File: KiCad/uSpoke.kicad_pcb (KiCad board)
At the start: 2 copper layers, 50 x 100 mm, 143 parts, among them J1 B2B-PH-K-S, J10 BL-A, J11 BL-C, J12 Amphenol 132289, J2 BAT+, J3 BAT-, J4 GCT USB4105/USB4110, J5 USB+, J6 USB-, J7 PLS-1x3, J8 PLS-1x6, J9 PLS-1x3, Q1 AO3407A, Q2 AO3407A, Q3 AO3400, Q4 AO3400, Q5 AO3400, Q6 AO3400, U1 SP0503BAHTG, U2 TP4056, U3 CP2102N-A02-GQFN28, U4 LM3671MF-3.3, U5 74HC4052PW, U6 STM32F103C8T6, U7 LSM303DLHC, X1 8MHz

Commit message: Draft PCB
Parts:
- removed A3: GM12864-01A, Spoke:GM12864-01A
- removed A4: G10A-F30, Spoke:G10A-F30
- removed A5: TU10-F, Spoke:TU10-F
- removed C10, C21, C3, C31, C33, C35, C4, C6: 100nF, Spoke:C0603
- removed C12, C9: ~, Spoke:C0603
- removed C2, C32, C7: 4.7uF, Spoke:C0805
- removed C24: 80 mF Supercap, Spoke:XH414HG-IV01E
- removed C29: 47uF, Spoke:C_tantA
- removed C34: 10uF, Spoke:C1206
- removed C36: 220nF, Spoke:C0603
- removed D6: BAT54C, Spoke:SOT-23
- removed H1: MountingHole, MountingHole:MountingHole_3.2mm_M3
- removed Q1: AO3407A, Spoke:SOT-23
- removed Q4, Q6: AO3400, Spoke:SOT-23
- removed R11, R14, R30, R37: 100kR, Spoke:R0603
- removed R12, R22, R24, R31, R8: 1kR, Spoke:R0603
- removed R16: ~, Spoke:R0603
- removed R18, R19, R20, R35, R36: 0R, Spoke:R0603
- removed R21, R40, R41: 3.9kR, Spoke:R0603
- removed R38: 300R, Spoke:R0603
- removed R39: 100R, Spoke:R1206
- removed SW1, SW2, SW3, SW4, SW5: ~, Spoke:Button_6x6
- removed TP1, TP12, TP13, TP14, TP15, TP16, TP17, TP18, TP3, TP4, TP5, TP6, TP7, TP8, TP9: Pad-Round, Spoke:Pad_round
- removed U3: CP2102N-A02-GQFN28, Spoke:QFN-28
- removed U7: LSM303DLHC, Spoke:LGA-14
- added J13: EXT, Spoke:Pad_oval, F.Cu at (37.3, 87.3)
- added J14: EXT, Spoke:Pad_oval, F.Cu at (37.3, 91.3)
- added REF**: SW_SPST_EVQP7A, Button_Switch_SMD:SW_SPST_EVQP7A, F.Cu at (163.1, 82.5)
- added REF**: SW_SPST_EVQP7A, Button_Switch_SMD:SW_SPST_EVQP7A, F.Cu at (163.2, 75.6)
- added REF**: SW_SPST_EVQP7A, Button_Switch_SMD:SW_SPST_EVQP7A, F.Cu at (163.0, 61.7)
- added REF**: SW_SPST_EVQP7A, Button_Switch_SMD:SW_SPST_EVQP7A, F.Cu at (162.9, 68.7)
- A1, A2, C1, C11, C13, C14, C15, C16, C17, C18, C19, C20, C22, C23, C25, C26, C27, C5, C8, D1, J12, L1, Q2, Q3, R13, R17, R23, R28, R32, R33, R34, R4, R7, R9, TP10, TP11, TP2, U2, U4, U5, U6, X1: moved to F.Cu
- D2, D4, D5: moved to B.Cu
- J10: value BL-A -> EXT
- J11: value BL-C -> EXT
- J2: value BAT+ -> PLS-1x3; footprint Spoke:Pad_oval -> Spoke:Header_1x3; moved to F.Cu
- J3: value BAT- -> EXT; moved to F.Cu
- J4: value GCT USB4105/USB4110 -> PLS-1x3; footprint Spoke:USB_C_16p_GCT4105 -> Spoke:Header_1x3; moved to F.Cu
- J5: value USB+ -> EXT
- J6: value USB- -> GND
- J7: value PLS-1x3 -> EXT; footprint Spoke:Header_1x3 -> Spoke:Pad_oval; moved to F.Cu
- J8: value PLS-1x6 -> EXT; footprint Spoke:Header_1x6 -> Spoke:Pad_oval; moved to F.Cu
- R1: value 5.1kR -> 100kR; moved to F.Cu
- R2: value 0R -> 100kR; moved to F.Cu
- R3: value 5.1kR -> 0R; moved to F.Cu
- R5: value 22.1kR -> 0R; moved to F.Cu
- R6: value 47.5kR -> 100kR; moved to F.Cu
- U1: footprint Spoke:SOT-143 -> Spoke:SOT-23-5; moved to F.Cu
- moved U1 167.2 mm to (2.79, 1.95), turned to 0 degrees
- moved D3 114.5 mm to (192.9, 89.0)
- moved LS1 114.5 mm to (189.4, 89.0)
- moved R29 114.5 mm to (186.9, 89.0)
- moved R32 113.5 mm to (192.3, 55.6), turned to 180 degrees
- moved TP10 113.5 mm to (192.3, 52.4), turned to 0 degrees
- moved A1 111.5 mm to (191.3, 63.9)
- moved TP11 108.0 mm to (189.6, 52.4), turned to 0 degrees
- moved R13 107.1 mm to (195.0, 73.6), turned to -90 degrees
- moved U5 106.3 mm to (190.5, 75.6), turned to -90 degrees
- moved C11 105.6 mm to (195.0, 77.6), turned to 90 degrees
- moved C23 105.5 mm to (188.3, 57.6), turned to 180 degrees
- moved TP2 104.8 mm to (185.0, 81.1)
- moved J3 103.5 mm to (37.3, 67.3)
- moved C25 103.5 mm to (187.3, 55.1), turned to 180 degrees
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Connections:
- net MUX_BLE_USB renamed MUX_BLE_EXT
- A1 pad 12: Net-(A1-TXD) -> BLE_TXD
- A1 pad 13: Net-(A1-LINK) -> unconnected-(A1-LINK-Pad13)
- A1 pad 15: Net-(A1-DATA) -> unconnected-(A1-DATA-Pad15)
- A1 pad 6: Net-(A1-DISC) -> unconnected-(A1-DISC-Pad6)
- A1 pad 7: Net-(A1-WAKEUP/SLEEP) -> GND
- A1 pad 9: Net-(A1-MODE) -> BLE_MODE
- A2 pad 8: Net-(A2-DIO2) -> unconnected-(A2-DIO2-Pad8)
- C1 pad 2: VBUS -> VEXT
- J10 pad 1: Net-(J10-Pad1) -> GPS_RXD
- J11 pad 1: Net-(Q6-D) -> GPS_PPS
- J2 pad 1: +BATT -> EXT_TXD
- J5 pad 1: VBUS -> VEXT
- J7 pad 1: USB_TXD -> +3V3
- J8 pad 1: +3V3 -> GPS_TXD
- Q2 pad 2: Net-(Q1-S) -> +BATT
- R1 pad 1: Net-(J4-CC2) -> Net-(Q5-G)
- R10 pad 2: VBUS -> VEXT
- R13 pad 1: VDD -> +3V3
- R2 pad 1: +BATT -> +3V3
- R2 pad 2: Net-(Q1-S) -> EXT_RXD
- R3 pad 1: Net-(J4-CC1) -> CONSOLE_TXD
- R3 pad 2: GND -> EXT_RXD
- R5 pad 1: VBUS -> CONSOLE_RXD
- R5 pad 2: Net-(U3-VBUS) -> EXT_TXD
- R6 pad 1: Net-(U3-VBUS) -> BOOT1
- R7 pad 1: Net-(Q1-S) -> +BATT
- U1 pad 2: /USB_DP -> EXT_TXD
- U1 pad 3: /USB_DN -> EXT_RXD
- U1 pad 4: VBUS -> VEXT
- U2 pad 4: VBUS -> VEXT
- U2 pad 8: VBUS -> VEXT
- U4 pad 4: Net-(U4-FB) -> +3V3
- U5 pad 11: GPS_RXD -> unconnected-(U5-1Y3-Pad11)
- U5 pad 14: USB_RXD -> EXT_RXD
- U5 pad 4: GPS_TXD -> unconnected-(U5-2Y3-Pad4)
- U5 pad 5: USB_TXD -> EXT_TXD
- U5 pad 9: Net-(U5-S1) -> GND
- U6 pad 11: LCD_BL -> GPS_PPS
- U6 pad 2: I2C_INT -> unconnected-(U6-PC13-Pad2)
- U6 pad 20: PPS_BOOT1 -> BOOT1
- U6 pad 25: LCD_CS -> unconnected-(U6-PB12-Pad25)
- U6 pad 26: LCD_SCK -> unconnected-(U6-PB13-Pad26)
- U6 pad 27: LCD_RESET -> unconnected-(U6-PB14-Pad27)
- U6 pad 28: LCD_MOSI -> unconnected-(U6-PB15-Pad28)
- U6 pad 29: LCD_DC -> unconnected-(U6-PA8-Pad29)
- U6 pad 30: Net-(U6-PA9) -> CONSOLE_TXD
- U6 pad 4: BTN_ALARM -> BLE_MODE
- U6 pad 42: I2C_SCL -> unconnected-(U6-PB6-Pad42)
- U6 pad 43: I2C_SDA -> unconnected-(U6-PB7-Pad43)
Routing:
- net +3V3: track 371.2 -> 0.00 mm, vias 25 -> 0
- net VBUS: track 154.2 -> 0.00 mm, vias 7 -> 0
- net GPS_TXD: track 102.7 -> 0.00 mm, vias 2 -> 0
- net GPS_RXD: track 97.2 -> 0.00 mm, vias 4 -> 0
- net USB_RXD: track 80.4 -> 0.00 mm, vias 1 -> 0
- net USB_TXD: track 79.2 -> 0.00 mm, vias 1 -> 0
- net VDD: track 74.2 -> 0.00 mm, vias 4 -> 0
- net VCC: track 72.9 -> 0.00 mm, vias 2 -> 0
- net BUZZER: track 66.1 -> 0.00 mm, vias 2 -> 0
- net BOOT0: track 64.3 -> 0.00 mm, vias 2 -> 0
- net Net-(D2-K): track 64.3 -> 0.00 mm, vias 2 -> 0
- net CONSOLE_RXD: track 61.4 -> 0.00 mm, vias 1 -> 0
- net CONSOLE_TXD: track 61.4 -> 0.00 mm, vias 1 -> 0
- net MCU_RESET: track 59.4 -> 0.00 mm, vias 1 -> 0
- net LED_GREEN: track 55.5 -> 0.00 mm, vias 1 -> 0
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- added copper zone on B.Cu, net VEXT
- removed copper zone on B.Cu, net GND
- removed copper zone on F.Cu, net GND
- removed copper zone on B.Cu, net VBUS
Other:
- board size 50 x 100 mm -> 35.9 x 61.1 mm

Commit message: Some progress
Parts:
- removed H2: MountingHole, MountingHole:MountingHole_3.2mm_M3
- removed REF** (x4): SW_SPST_EVQP7A, Button_Switch_SMD:SW_SPST_EVQP7A
- added J15: EXT, Spoke:Pad_oval, F.Cu at (201.1, 98.9)
- added R11: 0R, Spoke:R0603, F.Cu at (157.2, 74.7)
- added R8: 0R, Spoke:R0603, F.Cu at (157.2, 72.1)
- moved U1 171.0 mm to (153.5, 82.7)
- moved J1 81.9 mm to (190.8, 97.8), turned to 180 degrees
- moved TP2 27.7 mm to (159.0, 90.6)
- moved U5 26.5 mm to (216.9, 73.3)
- moved LS1 23.4 mm to (212.7, 91.4)
- moved D3 23.1 mm to (216.0, 88.8)
- moved R29 23.1 mm to (210.0, 88.8)
- moved L1 21.3 mm to (187.5, 86.2), turned to 90 degrees
- moved C13 19.5 mm to (183.5, 86.2), turned to 90 degrees
- moved R28 19.1 mm to (204.0, 70.6)
- moved D1 16.2 mm to (185.6, 97.1), turned to -90 degrees
- moved R32 14.9 mm to (177.5, 53.7), turned to -90 degrees
- moved TP10 14.8 mm to (180.7, 43.2), turned to 90 degrees
- moved C25 12.1 mm to (175.2, 56.0), turned to -90 degrees
- moved R9 12.0 mm to (181.3, 100.6), turned to 180 degrees
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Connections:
- U6 pad 2: unconnected-(U6-PC13-Pad2) -> Net-(U6-PC13)
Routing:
- removed copper zone on B.Cu, net +3V3
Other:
- board size 35.9 x 61.1 mm -> 30 x 50 mm

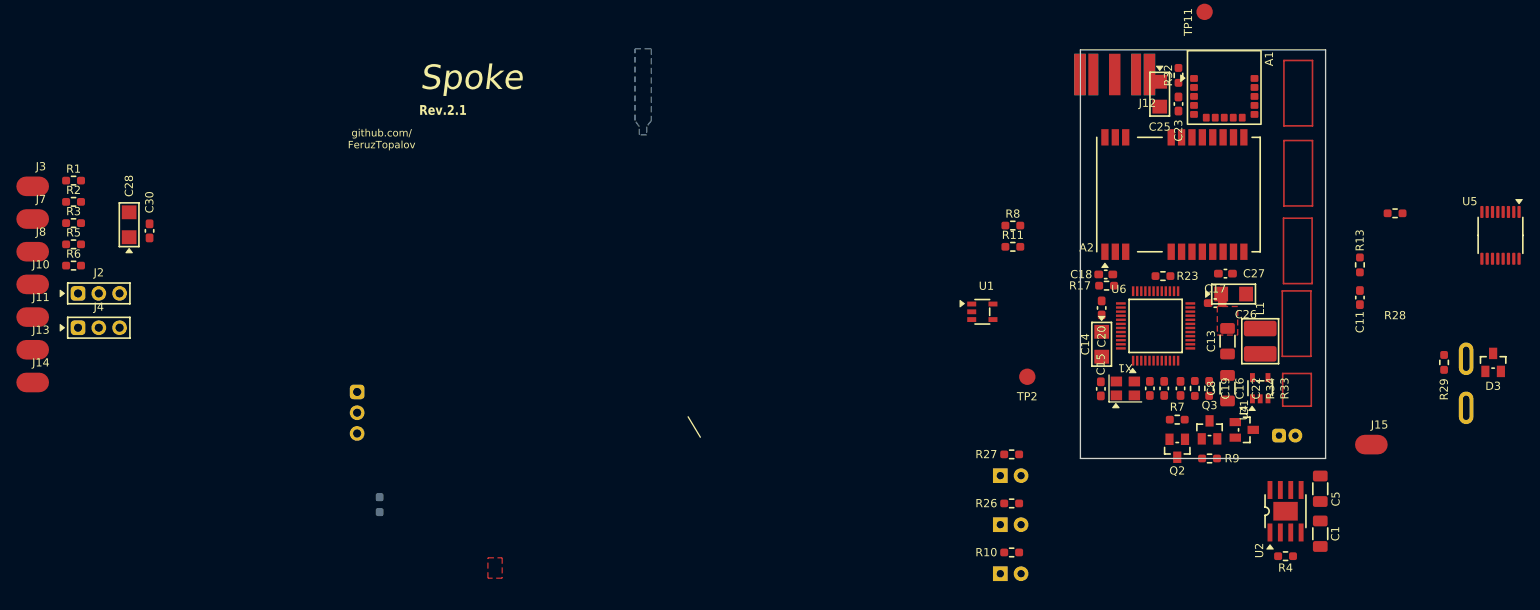
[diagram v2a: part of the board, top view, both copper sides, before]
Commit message: Some PCB planning
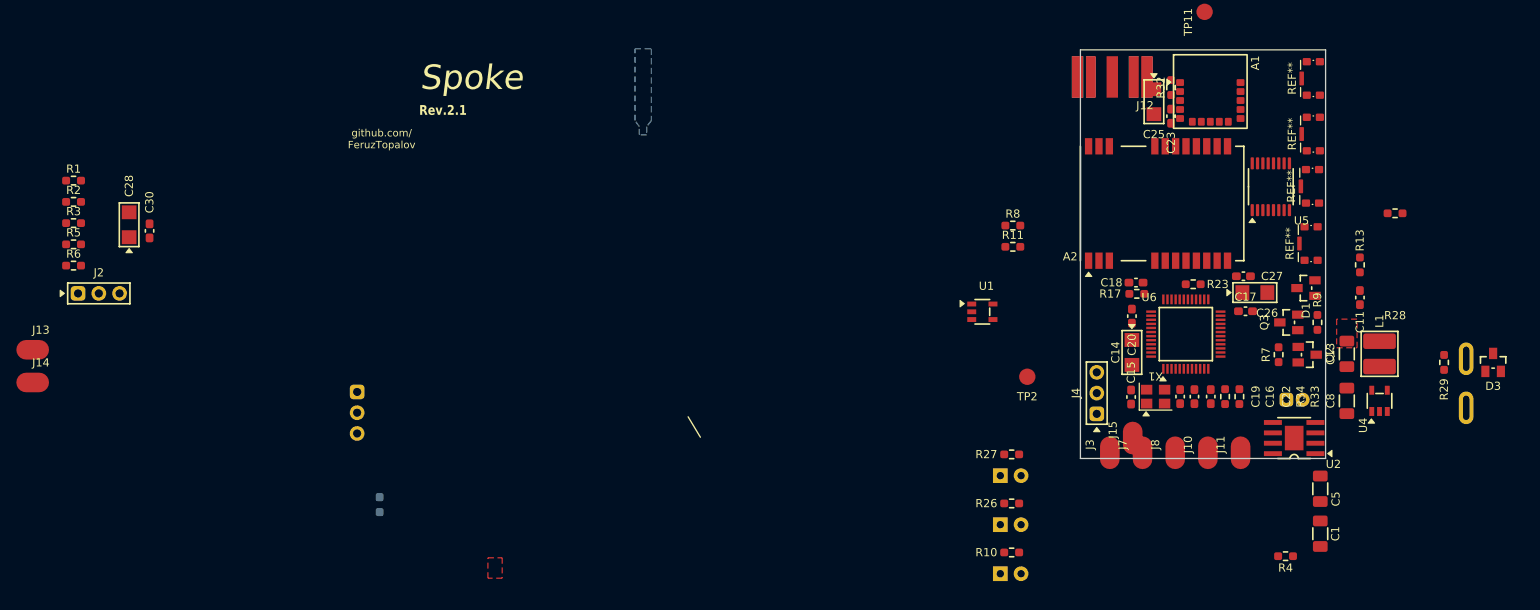
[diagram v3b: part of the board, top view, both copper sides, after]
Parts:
- added REF**: SW_SPST_CK_KMS2xxG, Button_Switch_SMD:SW_SPST_CK_KMS2xxG, F.Cu at (193.7, 74.3)
- added REF**: SW_SPST_CK_KMS2xxG, Button_Switch_SMD:SW_SPST_CK_KMS2xxG, F.Cu at (193.9, 67.3)
- added REF**: SW_SPST_CK_KMS2xxG, Button_Switch_SMD:SW_SPST_CK_KMS2xxG, F.Cu at (194.0, 54.1)
- added REF**: SW_SPST_CK_KMS2xxG, Button_Switch_SMD:SW_SPST_CK_KMS2xxG, F.Cu at (194.0, 60.9)
- moved J11 148.7 mm to (185.1, 99.9), turned to 90 degrees
- moved J10 145.3 mm to (181.1, 99.9), turned to 90 degrees
- moved J8 141.9 mm to (177.1, 99.9), turned to 90 degrees
- moved J7 138.8 mm to (173.1, 99.9), turned to 90 degrees
- moved J3 135.8 mm to (169.1, 99.9), turned to 90 degrees
- moved J4 122.4 mm to (167.5, 92.6), turned to 90 degrees
- moved J15 29.2 mm to (171.9, 98.1), turned to 90 degrees
- moved U5 28.7 mm to (188.8, 67.3), turned to 90 degrees
- moved R9 21.2 mm to (194.5, 84.0), turned to -90 degrees
- moved Q2 19.6 mm to (193.2, 87.9), turned to -90 degrees
- moved D1 18.9 mm to (193.1, 79.8), turned to 90 degrees
- moved Q3 16.3 mm to (191.0, 84.0), turned to 90 degrees
- moved R7 14.7 mm to (189.8, 87.9), turned to 90 degrees
- moved C13 14.7 mm to (198.1, 87.8)
- moved C8 14.7 mm to (198.1, 93.5)
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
